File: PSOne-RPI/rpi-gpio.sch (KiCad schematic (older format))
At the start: 3 parts, among them J12 Micro_SD_Card, J2 RaspberryPi4-ComputeModule, J8 GPIO

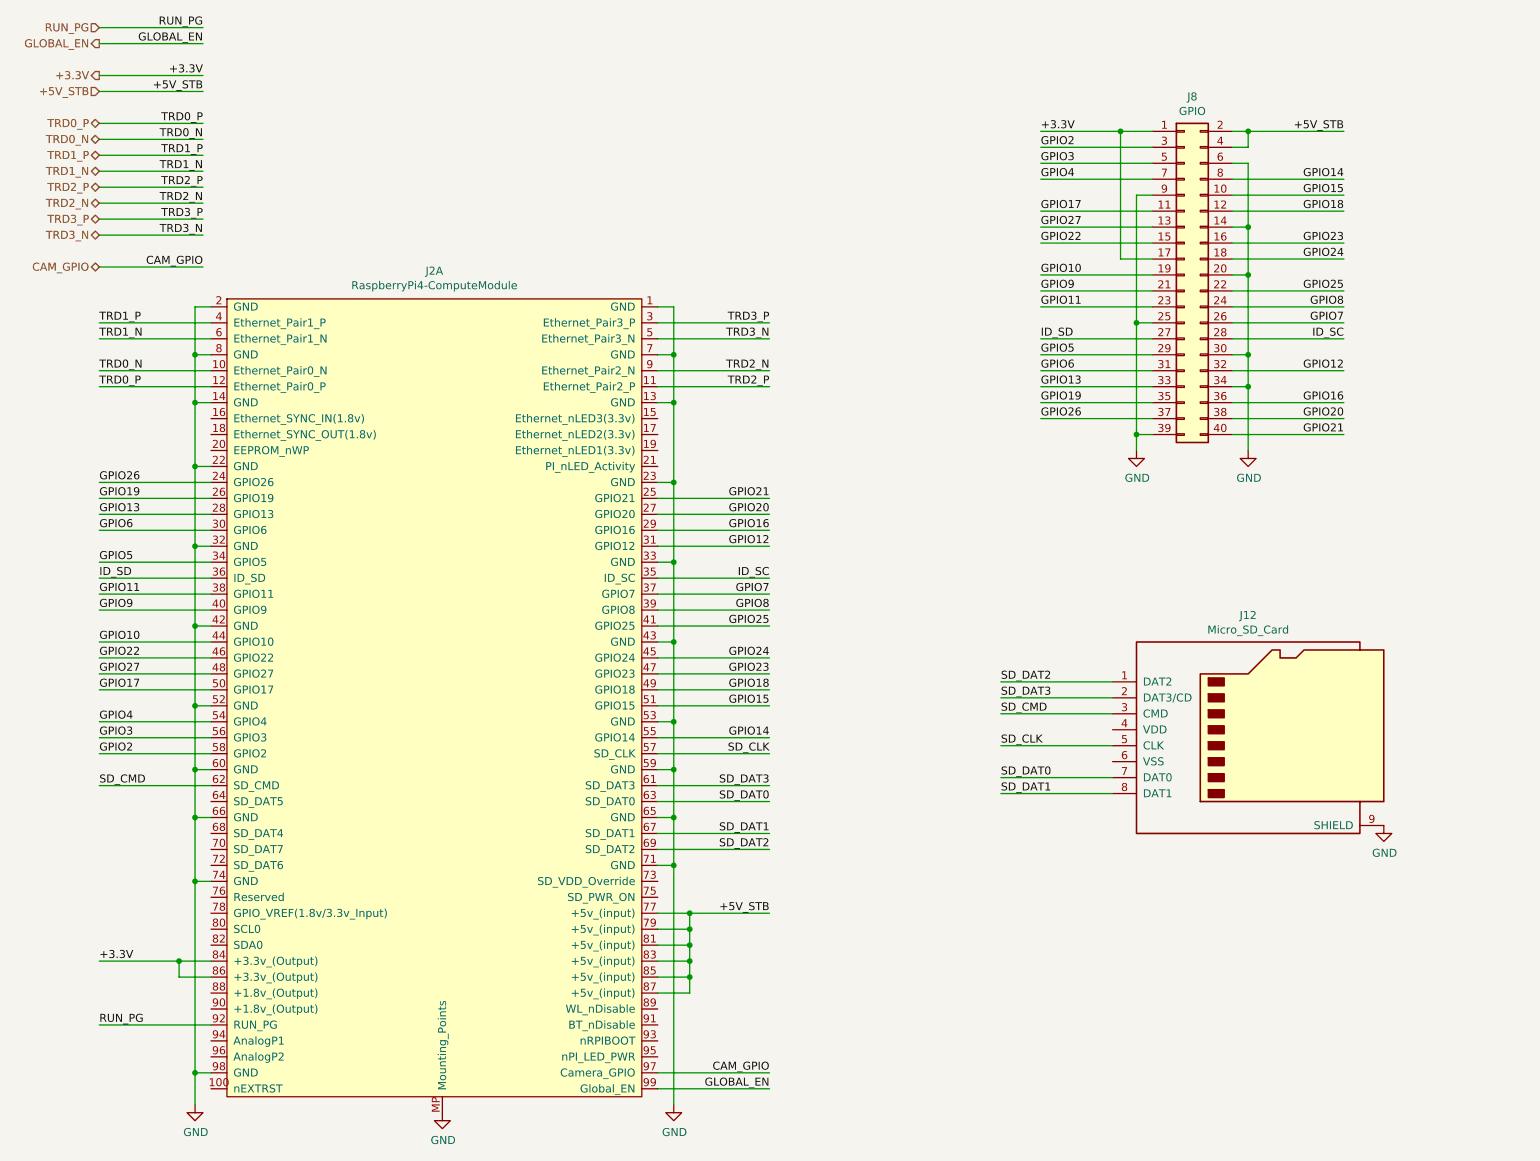
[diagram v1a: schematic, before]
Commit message: Added possibility to use the STM32 as RTC
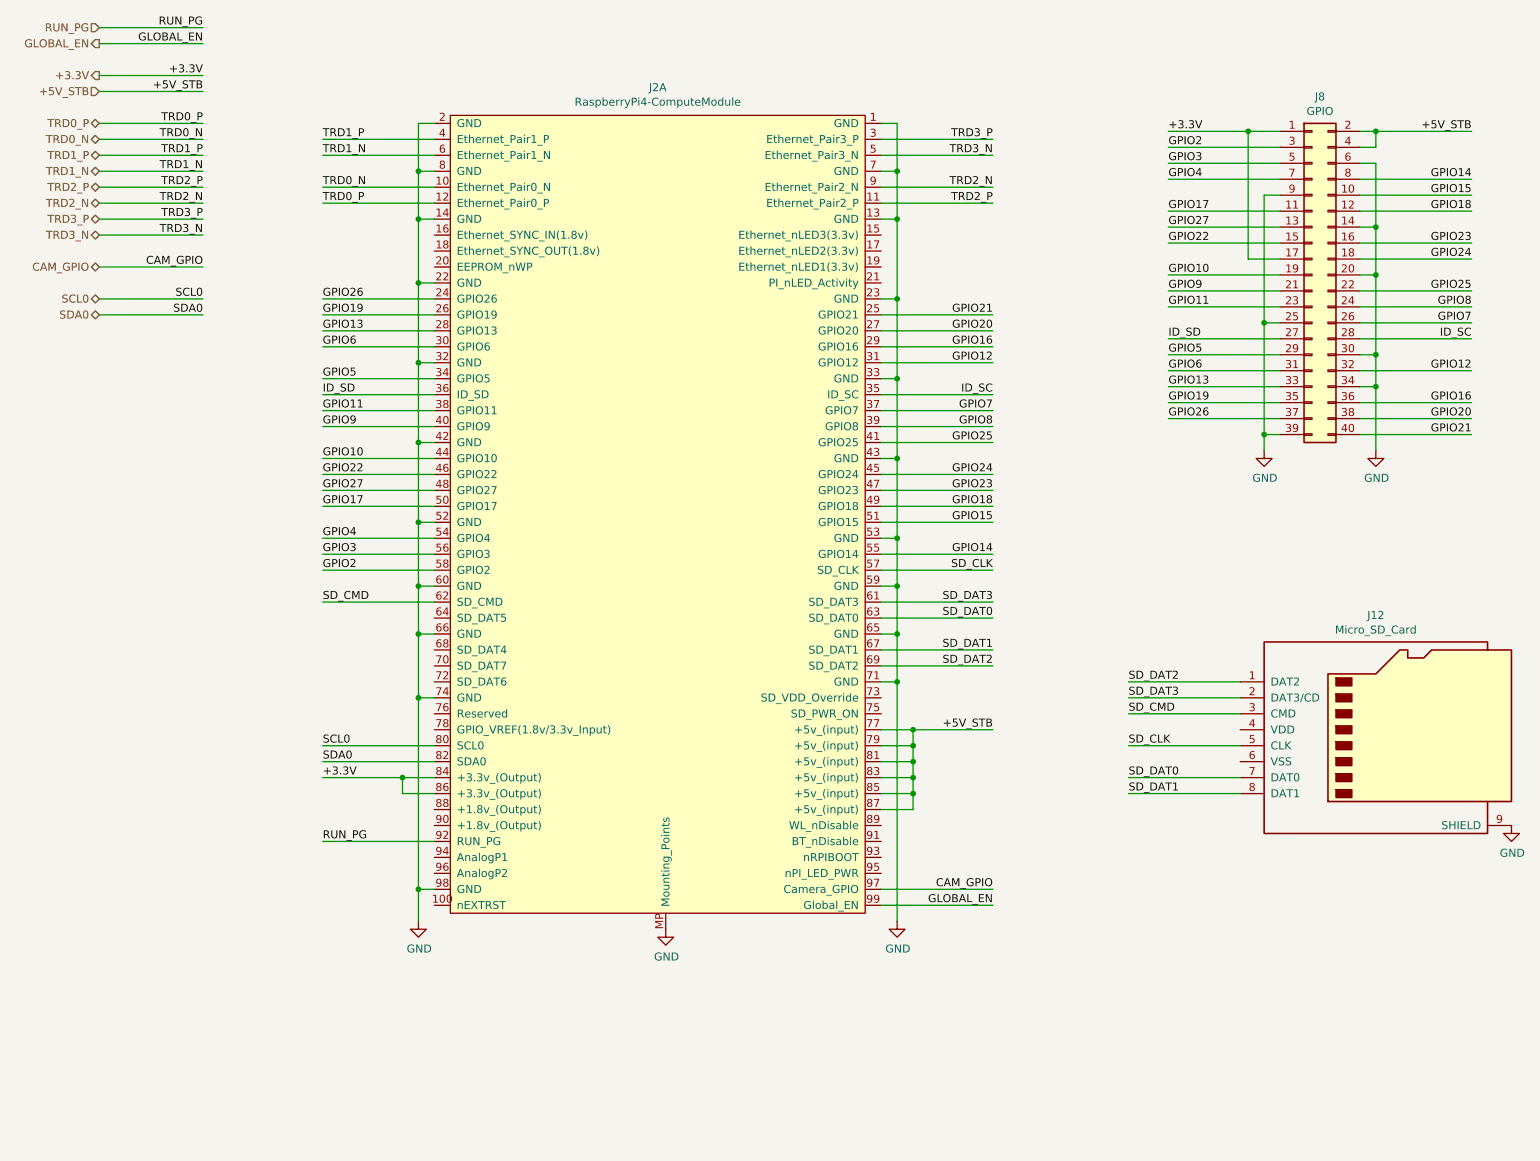
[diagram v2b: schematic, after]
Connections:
- net SCL0: now reaches J2.80 (SCL0)
- net SDA0: now reaches J2.82 (SDA0)
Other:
- moved on the sheet: J12, J2A, J8
